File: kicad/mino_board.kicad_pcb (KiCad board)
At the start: 2 copper layers, 224.8 x 91.4 mm, 39 parts, among them J1-2 Conn_01x04, J10 Conn_01x04, J2 Conn_01x05, J4 Conn_02x10_Counter_Clockwise, P1 LED, P2 LED, P3 LED, P4 LED, X1 SW_Push, Y1 SW_Push

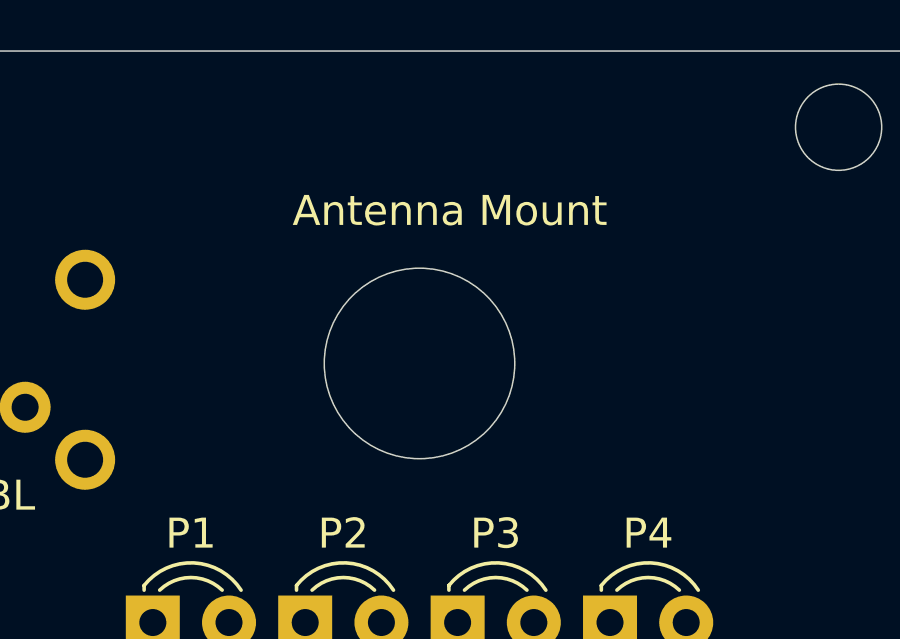
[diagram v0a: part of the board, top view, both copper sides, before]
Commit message: Remove Antenna Hole
Can better serve this with double sided tape and/or a flat antenna
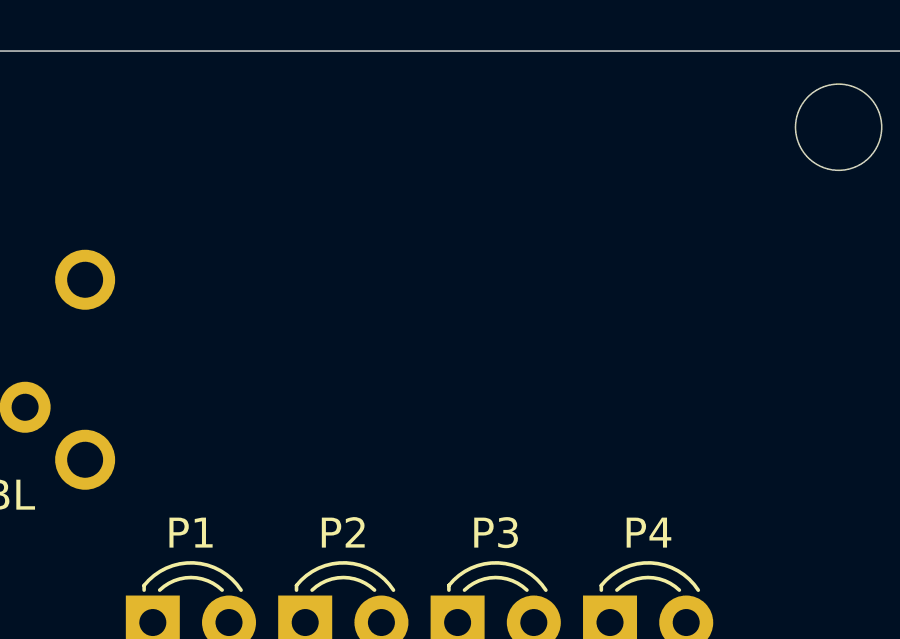
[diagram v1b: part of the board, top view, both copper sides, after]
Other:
- outline, holes or cut-outs redrawn
- board text removed: "Antenna Mount"
